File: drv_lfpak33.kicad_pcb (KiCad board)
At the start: 2 copper layers, 29 x 44 mm, 45 parts, among them J1 Conn_01x04_Male, J2 Conn_01x02_Male, J3 Conn_01x09_Male, J4 Conn_01x02_Male, Q1 PSMN1R8-30MLH, Q2 PSMN1R8-30MLH, Q3 PSMN1R8-30MLH, Q4 PSMN1R8-30MLH, Q5 PSMN1R8-30MLH, Q6 PSMN1R8-30MLH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

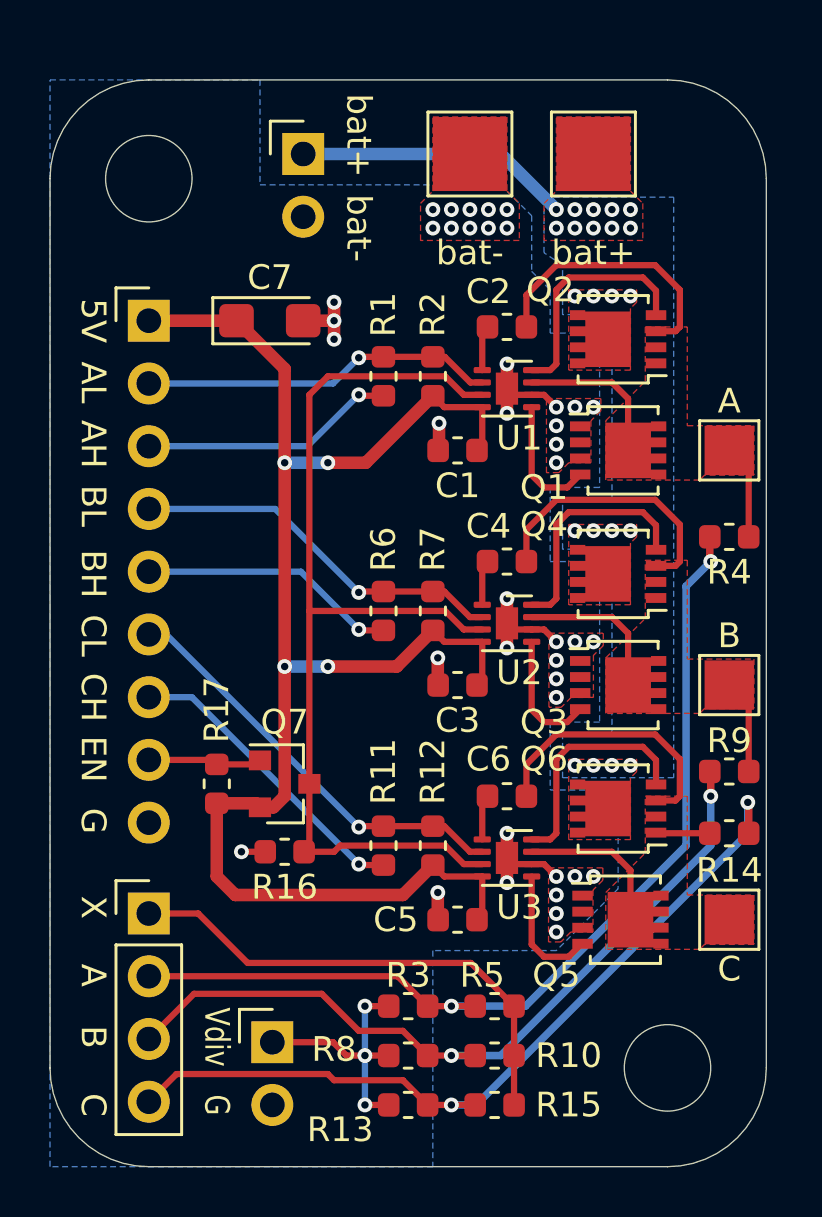
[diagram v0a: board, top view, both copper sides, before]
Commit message: update schematic: correct pull resistor values
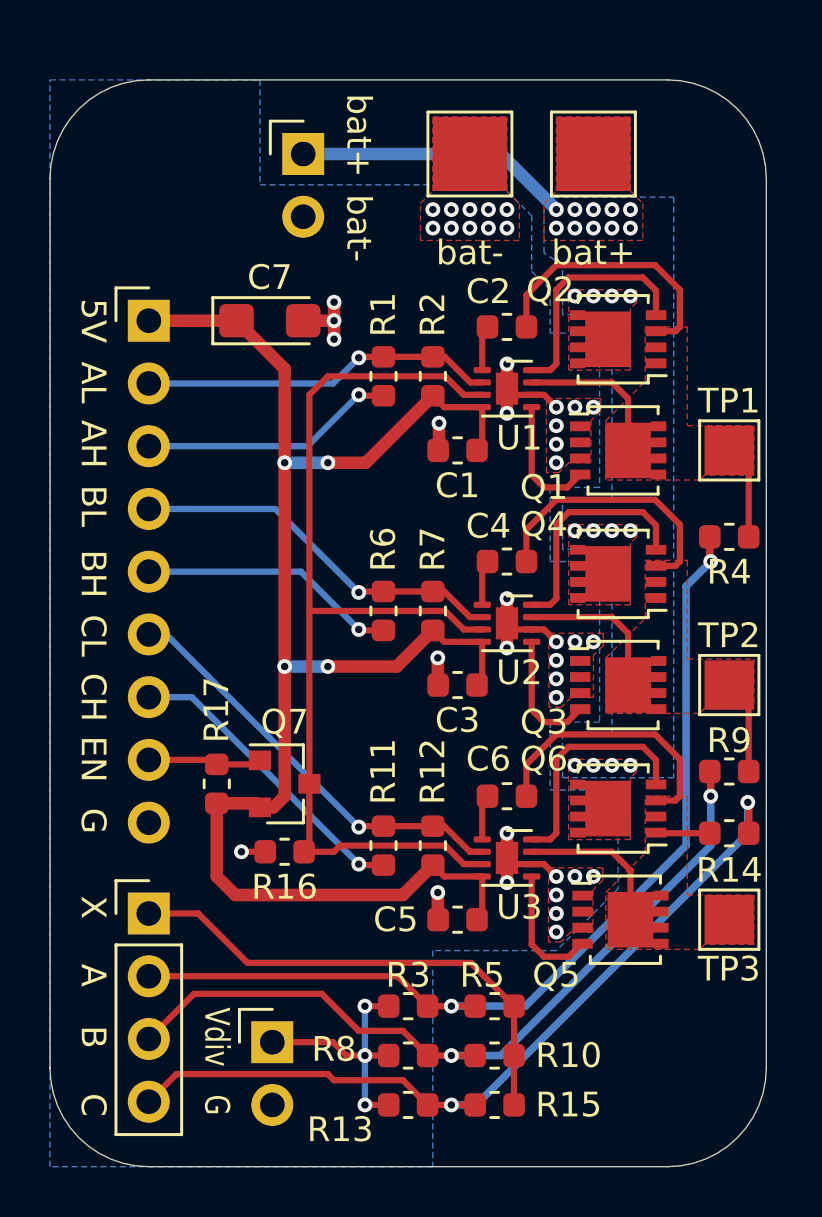
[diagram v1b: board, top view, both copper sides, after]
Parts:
- removed REF** (x2): MountingHole_3.5mm, MountingHole:MountingHole_3.5mm
- R1, R11, R6: value dnp (2k2) -> 2k7 (dnp)
- R12, R2, R7: value 8k66 (2k2) -> 3k9 (8k66)
- R16: value 2k2 -> 2k7
- renumbered A to TP1, B to TP2, C to TP3
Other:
- rule trace_min: 0.1 -> 0.2
- rule via_min_size: 0.4 -> 0.5

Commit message: update bottom silkscreen
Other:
- board text added: "crteensy NCP81xxx-3St-LFPAK33-breakout"

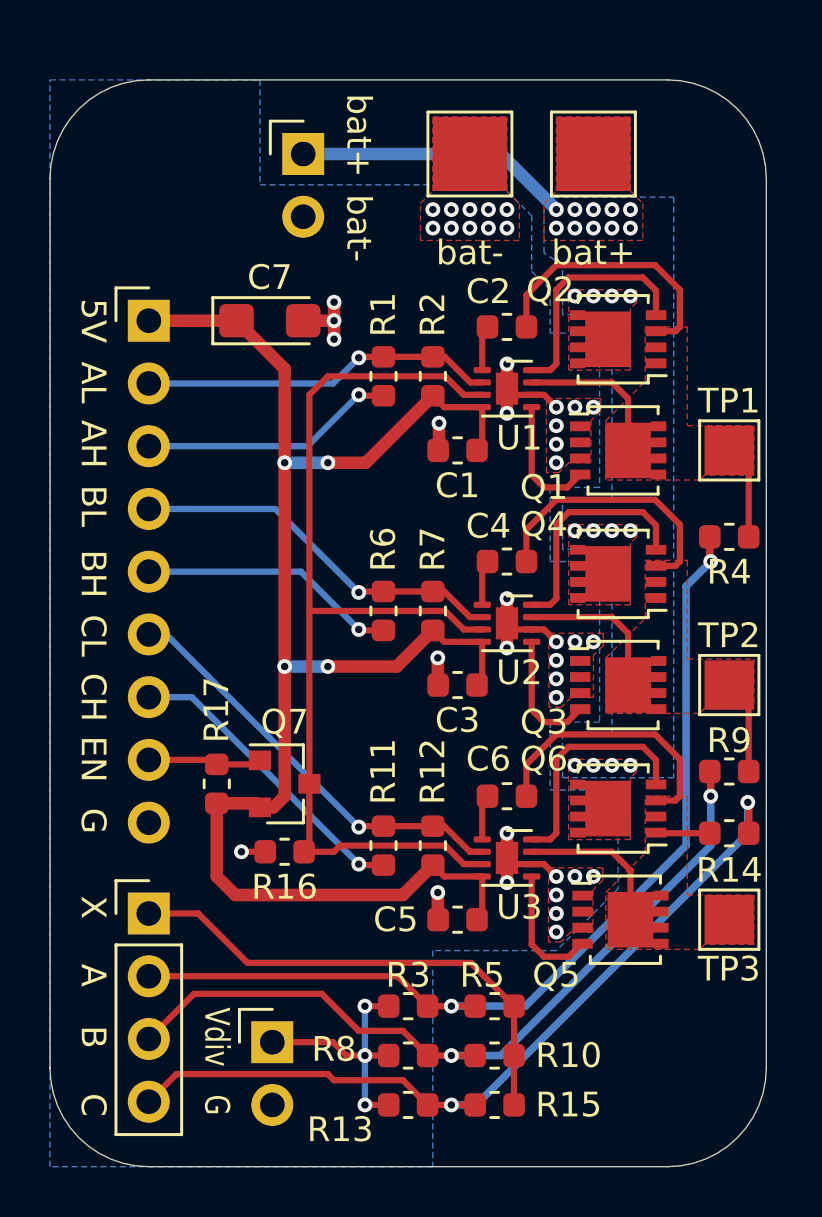
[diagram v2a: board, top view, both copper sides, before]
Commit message: add mounting holes
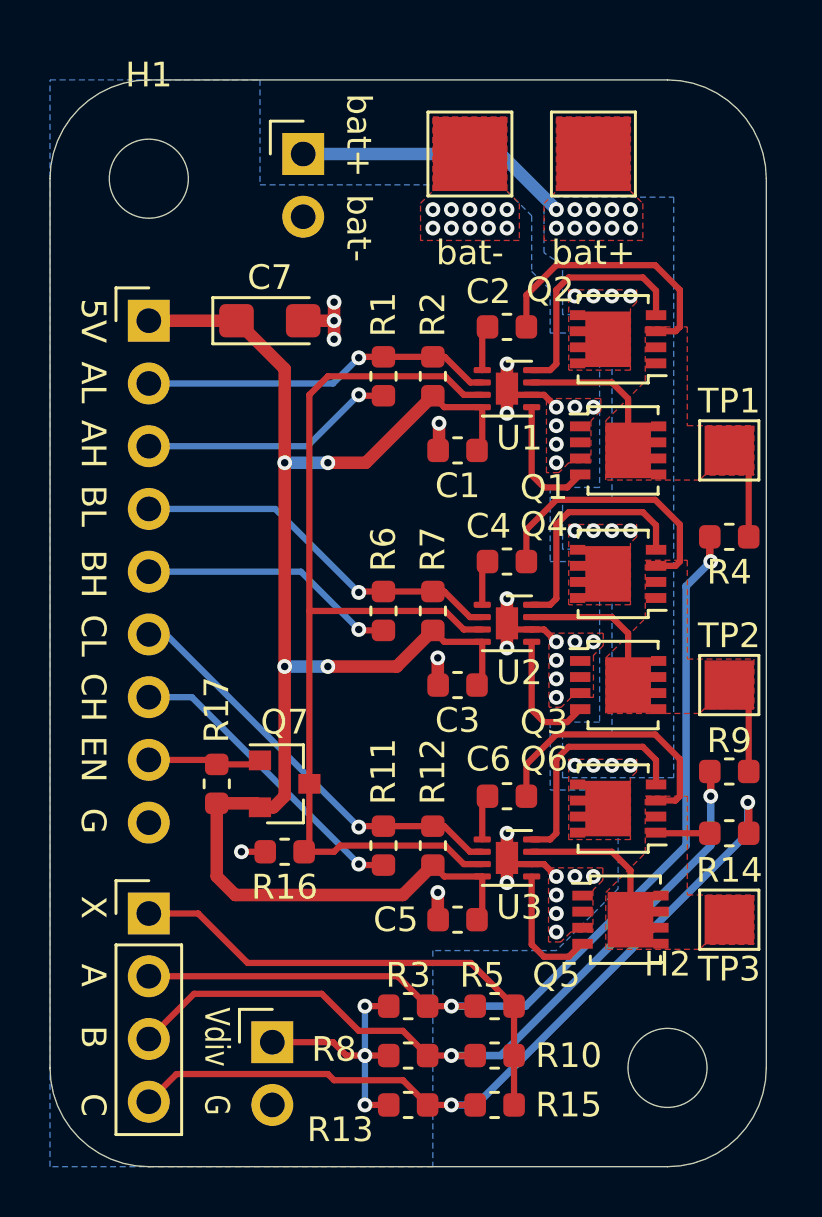
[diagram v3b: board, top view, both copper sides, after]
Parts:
- added H1: MountingHole, MountingHole:MountingHole_3.2mm_M3, F.Cu at (161.0, 62.0)
- added H2: MountingHole, MountingHole:MountingHole_3.2mm_M3, F.Cu at (182.0, 98.0)
